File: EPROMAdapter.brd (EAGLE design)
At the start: 160 x 100 mm, 2 parts

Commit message: wrapped that up
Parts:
- renumbered EPROM to 2716, U$1 to 2513
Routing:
- added copper zone on layer 1, net GND
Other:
- board size 160 x 100 mm -> 26.1 x 33.1 mm
- board text added: "2513 Character Gen. to 2716 EPROM Adapter"
- board text added: "github.com/bbenchoff/2513CharGenAdapter"
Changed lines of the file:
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@@
 <layer number="44" name="Drills" color="7" fill="1" visible="no" active="yes"/>
 <layer number="45" name="Holes" color="7" fill="1" visible="no" active="yes"/>
-<layer number="46" name="Milling" color="3" fill="1" visible="no" active="yes"/>
+<layer number="46" name="Milling" color="3" fill="1" visible="yes" active="yes"/>
 <layer number="47" name="Measures" color="7" fill="1" visible="no" active="yes"/>
 <layer number="48" name="Document" color="7" fill="1" visible="yes" active="yes"/>
@@
 <board>
 <plain>
-<wire x1="0" y1="0" x2="160" y2="0" width="0" layer="20"/>
-<wire x1="160" y1="0" x2="160" y2="100" width="0" layer="20"/>
-<wire x1="160" y1="100" x2="0" y2="100" width="0" layer="20"/>
-<wire x1="0" y1="100" x2="0" y2="0" width="0" layer="20"/>
-<text x="73.66" y="34.29" size="1.778" layer="22" font="vector" ratio="20" rot="MR270">Bottom towards board</text>
+<wire x1="59.055" y1="5.08" x2="85.07" y2="5.08" width="0" layer="20"/>
+<wire x1="85.07" y1="5.08" x2="85.197" y2="38.151" width="0" layer="20"/>
+<wire x1="85.197" y1="38.151" x2="59.182" y2="38.151" width="0" layer="20"/>
+<wire x1="59.182" y1="38.151" x2="59.055" y2="5.08" width="0" layer="20"/>
+<text x="75.819" y="34.29" size="1.778" layer="22" font="vector" ratio="20" rot="MR270">Bottom towards board</text>
+<text x="72.644" y="7.493" size="1.778" layer="27" font="vector" ratio="20" rot="R90">2513 Character Gen.
+to 2716 EPROM Adapter</text>
+<text x="83.82" y="33.02" size="0.8128" layer="27" font="vector" ratio="14" rot="R270">github.com/bbenchoff/2513CharGenAdapter</text>
+<wire x1="59.182" y1="37.846" x2="85.09" y2="37.846" width="0.4064" layer="46"/>
+<wire x1="85.09" y1="37.846" x2="85.09" y2="5.08" width="0.4064" layer="46"/>
+<wire x1="85.09" y1="5.08" x2="59.182" y2="5.08" width="0.4064" layer="46"/>
+<wire x1="59.182" y1="5.08" x2="59.182" y2="37.846" width="0.4064" layer="46"/>
 </plain>
 <attributes>
@@
 </autorouter>
 <elements>
-<element name="EPROM" library="memory" library_urn="urn:adsk.eagle:library:279" package="DIL24" package3d_urn="urn:adsk.eagle:package:19955/2" value="" x="73.66" y="21.59" smashed="yes" rot="R270">
+<element name="2716" library="memory" library_urn="urn:adsk.eagle:library:279" package="DIL24" package3d_urn="urn:adsk.eagle:package:19955/2" value="" x="73.66" y="21.59" smashed="yes" rot="R270">
 <attribute name="NAME" x="66.929" y="37.084" size="1.778" layer="25" ratio="10"/>
 <attribute name="VALUE" x="72.771" y="32.893" size="1.778" layer="27" ratio="10" rot="R270"/>
 </element>
-<element name="U$1" library="memory" package="DIL24" package3d_urn="urn:adsk.eagle:package:19955/2" value="2513-CHARACTER" x="69.85" y="21.59" smashed="yes" rot="R270">
+<element name="2513" library="memory" package="DIL24" package3d_urn="urn:adsk.eagle:package:19955/2" value="2513-CHARACTER" x="69.85" y="21.59" smashed="yes" rot="R270">
 <attribute name="NAME" x="63.119" y="37.084" size="1.778" layer="25" ratio="10"/>
 </element>
@@
 <signals>
 <signal name="VCC">
-<contactref element="U$1" pad="24"/>
-<contactref element="EPROM" pad="24"/>
+<contactref element="2513" pad="24"/>
+<contactref element="2716" pad="24"/>
 <wire x1="77.47" y1="35.56" x2="81.28" y2="35.56" width="0.4064" layer="1"/>
 </signal>
 <signal name="GND">
-<contactref element="U$1" pad="10"/>
-<contactref element="EPROM" pad="12"/>
-<contactref element="EPROM" pad="22"/>
-<contactref element="EPROM" pad="19"/>
-<wire x1="81.28" y1="22.86" x2="81.28" y2="30.48" width="0" layer="19" extent="1-1"/>
-<wire x1="62.23" y1="12.7" x2="81.28" y2="22.86" width="0" layer="19" extent="1-1"/>
-<wire x1="66.04" y1="7.62" x2="81.28" y2="22.86" width="0" layer="19" extent="1-1"/>
+<contactref element="2513" pad="10"/>
+<contactref element="2716" pad="12"/>
+<contactref element="2716" pad="22"/>
+<contactref element="2716" pad="19"/>
+<polygon width="0.4064" layer="1">
+<vertex x="59.055" y="37.719"/>
+<vertex x="85.09" y="37.719"/>
+<vertex x="85.09" y="5.08"/>
+<vertex x="59.055" y="5.08"/>
+</polygon>
 </signal>
 <signal name="A8">
-<contactref element="U$1" pad="22"/>
-<contactref element="EPROM" pad="23"/>
+<contactref element="2513" pad="22"/>
+<contactref element="2716" pad="23"/>
 <wire x1="81.28" y1="33.02" x2="77.47" y2="30.48" width="0.4064" layer="1"/>
 </signal>
 <signal name="A7">
-<contactref element="U$1" pad="21"/>
-<contactref element="EPROM" pad="1"/>
+<contactref element="2513" pad="21"/>
+<contactref element="2716" pad="1"/>
 <wire x1="66.04" y1="35.56" x2="77.47" y2="27.94" width="0.4064" layer="1"/>
 </signal>
 <signal name="A6">
-<contactref element="U$1" pad="20"/>
-<contactref element="EPROM" pad="2"/>
+<contactref element="2513" pad="20"/>
+<contactref element="2716" pad="2"/>
 <wire x1="66.04" y1="33.02" x2="77.47" y2="25.4" width="0.4064" layer="1"/>
 </signal>
 <signal name="A5">
-<contactref element="U$1" pad="19"/>
-<contactref element="EPROM" pad="3"/>
+<contactref element="2513" pad="19"/>
+<contactref element="2716" pad="3"/>
 <wire x1="66.04" y1="30.48" x2="77.47" y2="22.86" width="0.4064" layer="1"/>
 </signal>
 <signal name="A4">
-<contactref element="U$1" pad="18"/>
-<contactref element="EPROM" pad="4"/>
+<contactref element="2513" pad="18"/>
+<contactref element="2716" pad="4"/>
 <wire x1="66.04" y1="27.94" x2="77.47" y2="20.32" width="0.4064" layer="1"/>
 </signal>
 <signal name="A3">
-<contactref element="U$1" pad="17"/>
-<contactref element="EPROM" pad="5"/>
+<contactref element="2513" pad="17"/>
+<contactref element="2716" pad="5"/>
 <wire x1="66.04" y1="25.4" x2="77.47" y2="17.78" width="0.4064" layer="1"/>
 </signal>
 <signal name="A2">
-<contactref element="U$1" pad="16"/>
-<contactref element="EPROM" pad="6"/>
+<contactref element="2513" pad="16"/>
+<contactref element="2716" pad="6"/>
 <wire x1="66.04" y1="22.86" x2="77.47" y2="15.24" width="0.4064" layer="1"/>
 </signal>
 <signal name="A1">
-<contactref element="U$1" pad="15"/>
-<contactref element="EPROM" pad="7"/>
+<contactref element="2513" pad="15"/>
+<contactref element="2716" pad="7"/>
 <wire x1="66.04" y1="20.32" x2="77.47" y2="12.7" width="0.4064" layer="1"/>
 </signal>
 <signal name="A0">
-<contactref element="U$1" pad="14"/>
-<contactref element="EPROM" pad="8"/>
+<contactref element="2513" pad="14"/>
+<contactref element="2716" pad="8"/>
 <wire x1="66.04" y1="17.78" x2="77.47" y2="10.16" width="0.4064" layer="1"/>
 </signal>
 <signal name="D1">
-<contactref element="U$1" pad="4"/>
-<contactref element="EPROM" pad="9"/>
+<contactref element="2513" pad="4"/>
+<contactref element="2716" pad="9"/>
 <wire x1="66.04" y1="15.24" x2="67.31" y2="15.24" width="0.4064" layer="16"/>
 <wire x1="71.12" y1="19.05" x2="71.12" y2="25.4" width="0.4064" layer="16"/>
@@
 </signal>
 <signal name="D2">
-<contactref element="U$1" pad="5"/>
-<contactref element="EPROM" pad="10"/>
+<contactref element="2513" pad="5"/>
+<contactref element="2716" pad="10"/>
 <wire x1="62.23" y1="25.4" x2="63.5" y2="24.13" width="0.4064" layer="16"/>
 <wire x1="63.5" y1="24.13" x2="68.58" y2="24.13" width="0.4064" layer="16"/>
@@
 </signal>
 <signal name="D3">
-<contactref element="U$1" pad="6"/>
-<contactref element="EPROM" pad="11"/>
+<contactref element="2513" pad="6"/>
+<contactref element="2716" pad="11"/>
 <wire x1="66.04" y1="10.16" x2="67.818" y2="10.16" width="0.4064" layer="16"/>
 <wire x1="67.818" y1="10.16" x2="72.263" y2="14.605" width="0.4064" layer="16"/>
@@
 </signal>
 <signal name="D4">
-<contactref element="U$1" pad="7"/>
-<contactref element="EPROM" pad="13"/>
+<contactref element="2513" pad="7"/>
+<contactref element="2716" pad="13"/>
 <wire x1="62.23" y1="20.32" x2="64.262" y2="18.288" width="0.4064" layer="16"/>
 <wire x1="64.262" y1="18.288" x2="64.262" y2="14.224" width="0.4064" layer="16"/>
@@
 </signal>
 <signal name="D5">
-<contactref element="U$1" pad="8"/>
-<contactref element="EPROM" pad="14"/>
+<contactref element="2513" pad="8"/>
+<contactref element="2716" pad="14"/>
 <wire x1="81.28" y1="10.16" x2="80.264" y2="9.144" width="0.4064" layer="16"/>
 <wire x1="64.95875625" y1="9.144" x2="64.3636" y2="9.73915625" width="0.4064" layer="16"/>
@@
 </signal>
 <signal name="!CE">
-<contactref element="EPROM" pad="18"/>
-<contactref element="EPROM" pad="20"/>
-<contactref element="U$1" pad="11"/>
+<contactref element="2716" pad="18"/>
+<contactref element="2716" pad="20"/>
+<contactref element="2513" pad="11"/>
 <wire x1="62.23" y1="10.16" x2="63.627" y2="8.763" width="0.4064" layer="1"/>
 <wire x1="69.723" y1="8.763" x2="71.374" y2="10.414" width="0.4064" layer="1"/>
@@
 </drawing>
 <compatibility>
+<note version="6.3" minversion="6.2.2" severity="warning">
+Since Version 6.2.2 text objects can contain more than one line,
+which will not be processed correctly with this version.
+</note>
 <note version="8.2" severity="warning">
 Since Version 8.2, EAGLE supports online libraries. The ids

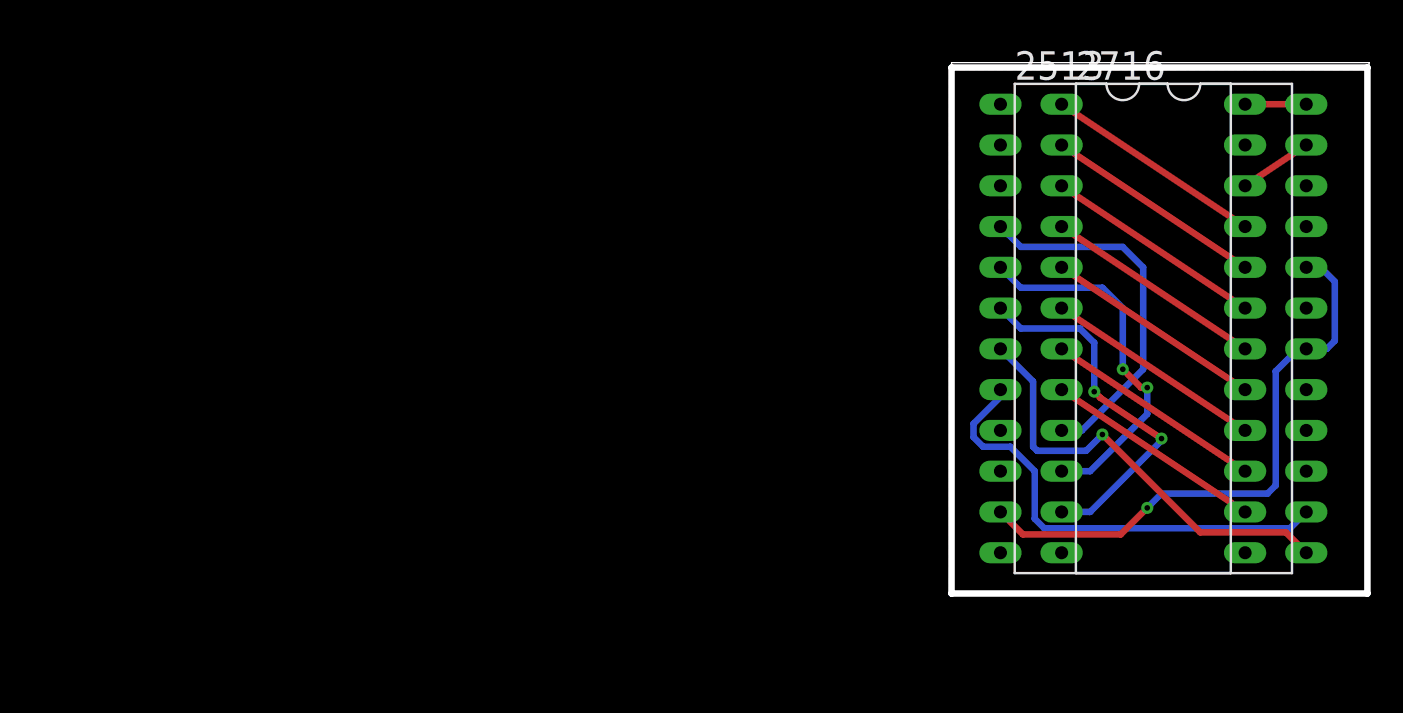
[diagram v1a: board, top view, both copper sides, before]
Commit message: fixed silkscreen on board; added oshpark link to readme
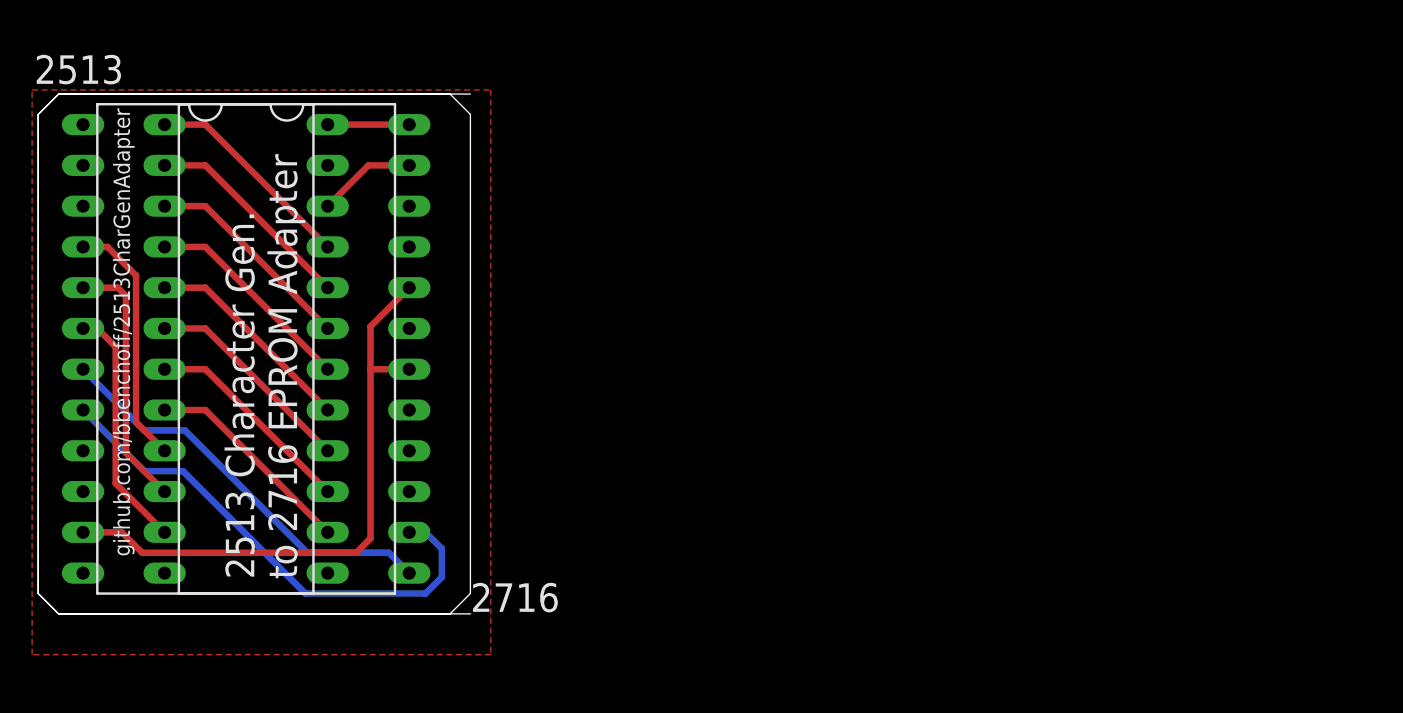
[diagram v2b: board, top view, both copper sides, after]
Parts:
- moved 2513 57.2 mm to (12.7, 20.3)
- moved 2716 55.9 mm to (17.8, 20.3)
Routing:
- net D3: track 23.1 -> 15.3 mm, vias 2 -> 0
- net D1: track 23.0 -> 15.7 mm
- net D2: track 22.9 -> 16.1 mm, vias 2 -> 0
- net D5: track 28.9 -> 31.7 mm
- net D4: track 27.5 -> 25.6 mm, vias 1 -> 0
- net A8: track 4.58 -> 6.13 mm
- net !CE: track 36.4 -> 37.8 mm, vias 1 -> 0
- net VCC: track 3.81 -> 5.08 mm
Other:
- board size 26.1 x 33.1 mm -> 26.9 x 32.4 mm
